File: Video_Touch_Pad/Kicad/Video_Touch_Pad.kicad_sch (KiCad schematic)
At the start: 15 parts, among them J1 DE9

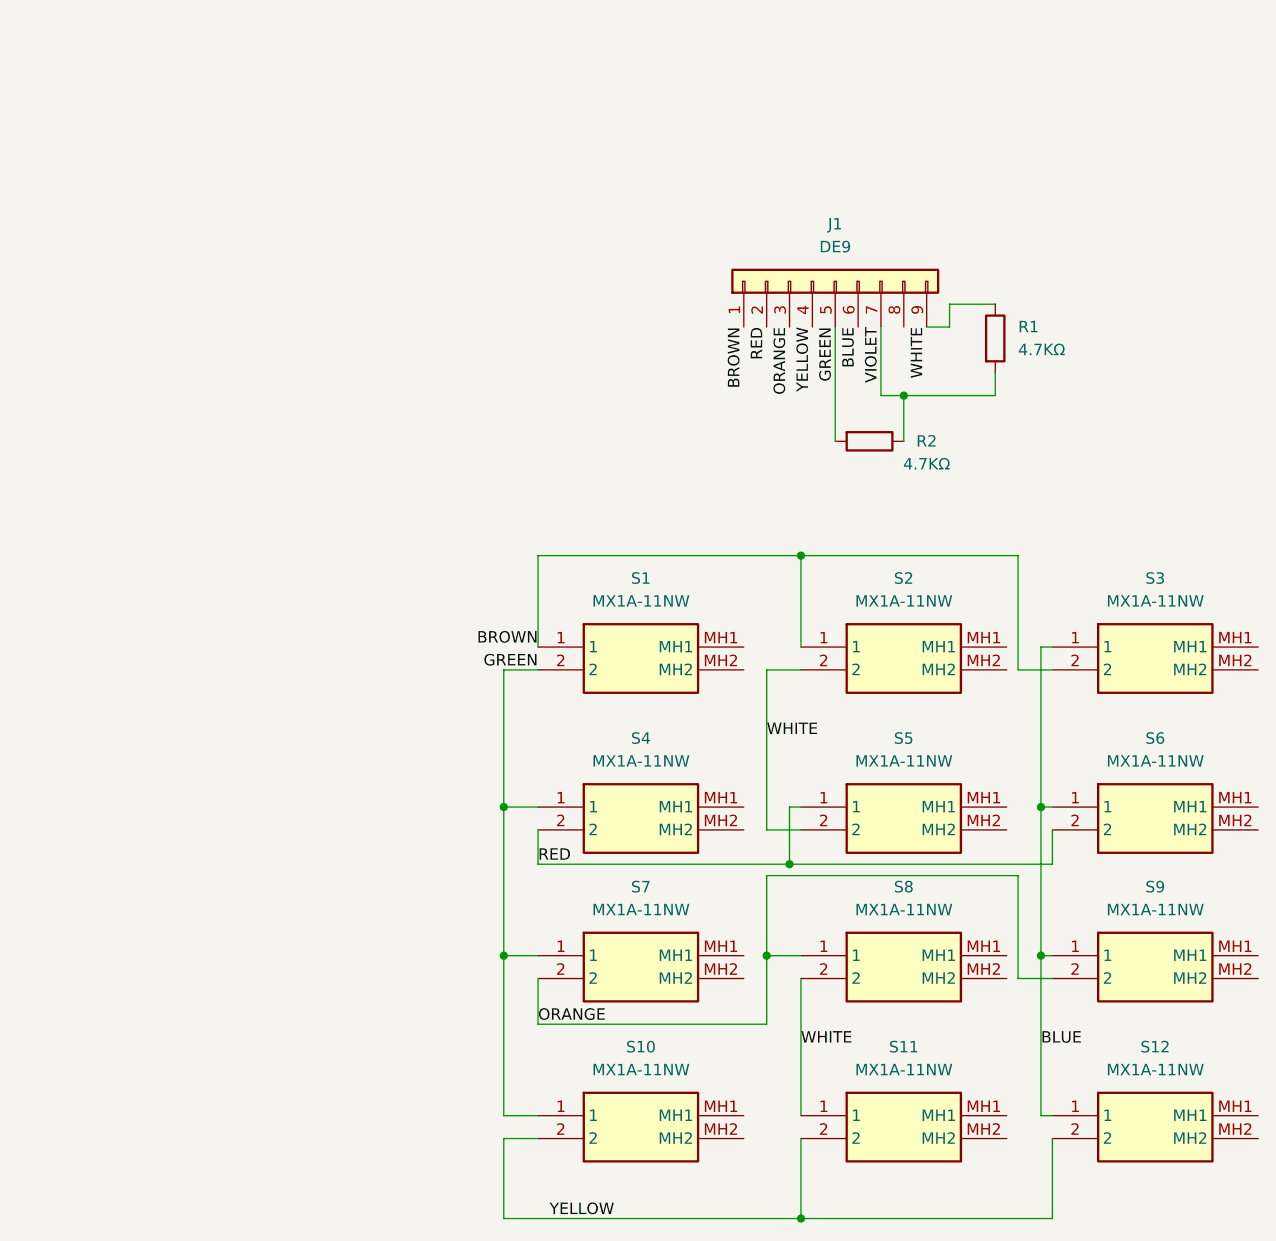
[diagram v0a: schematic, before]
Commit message: Added mounting holes
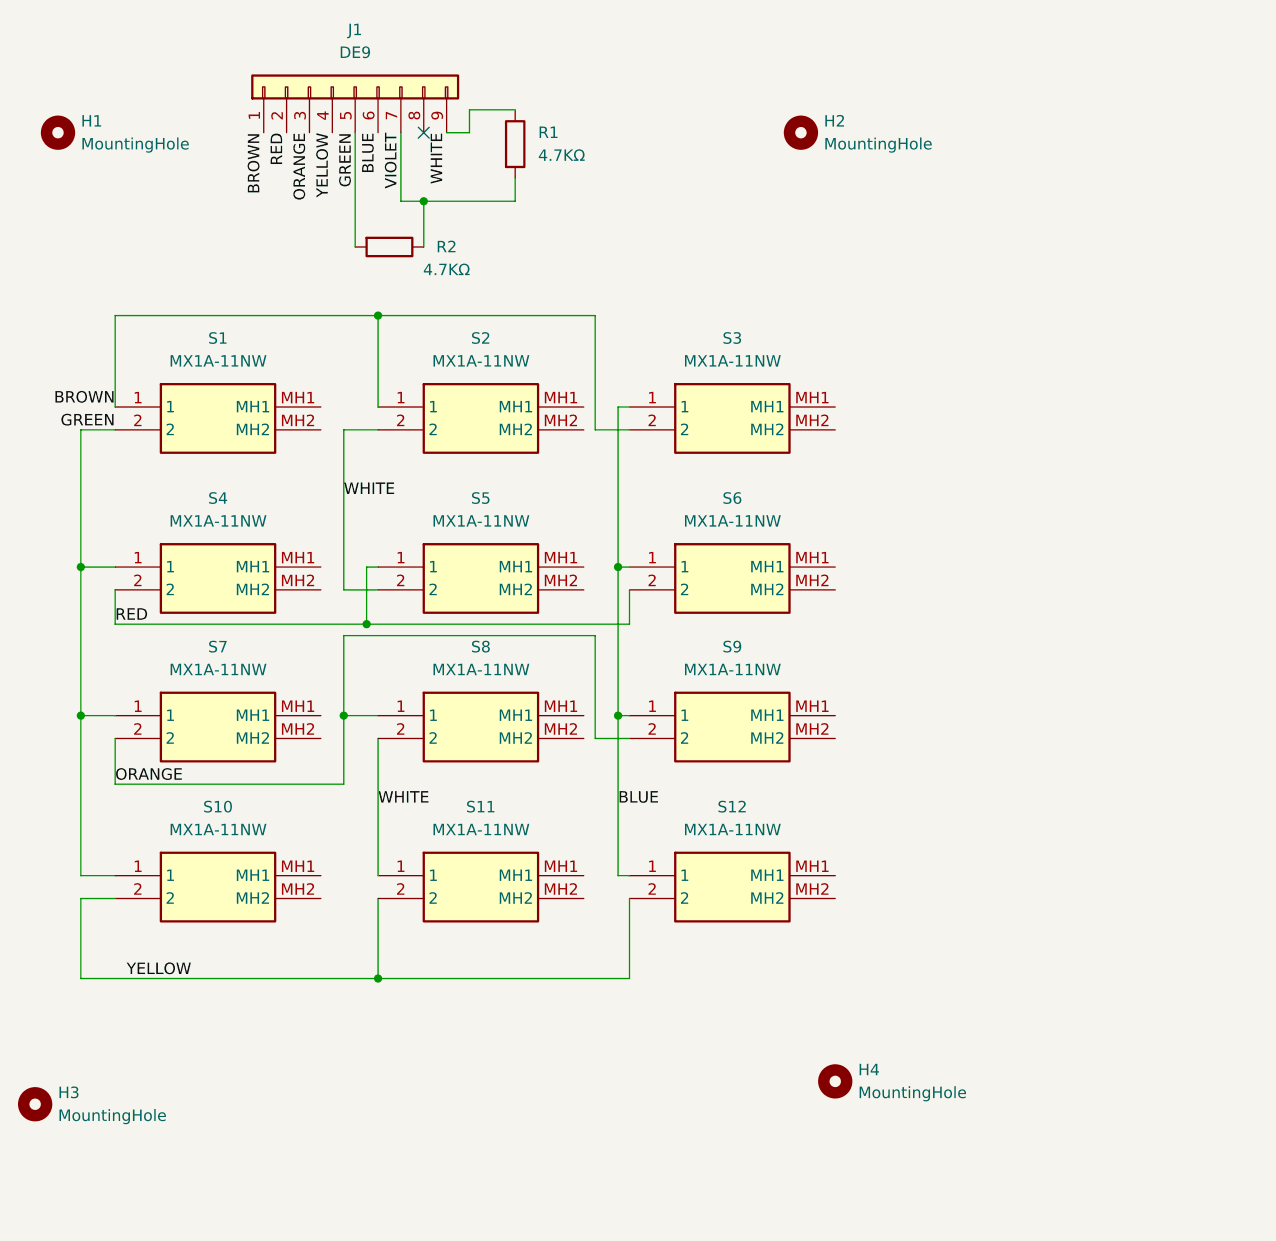
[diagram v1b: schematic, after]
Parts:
- added H1, H2, H3, H4: MountingHole, MountingHole:MountingHole_3.2mm_M3, symbol Mechanical:MountingHole
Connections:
- no-connect marks 0 -> 1
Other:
- moved on the sheet: J1, R1, R2, S1, S10, S11, S12, S2, S3, S4, S5, S6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
